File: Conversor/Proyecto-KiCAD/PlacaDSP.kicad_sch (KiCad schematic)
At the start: 0 parts

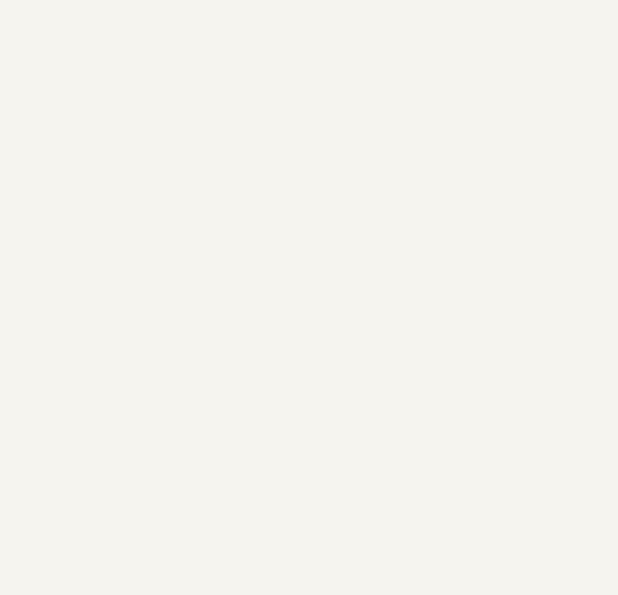
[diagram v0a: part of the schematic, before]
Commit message: Comenzar a pasar la placa adaptadora al proyecto
- Agregar a bibliografia info sobre la ControlCARD del TMS320F28335
(pinout del DIMM100 incluido)
- Agregar el proyecto importado a KiCad de la placa adaptadora
Por hacer:
  - Terminar de pasar la placa adaptadora, viendo que cosas no son
necesarias (como la entrada de 12V separada)
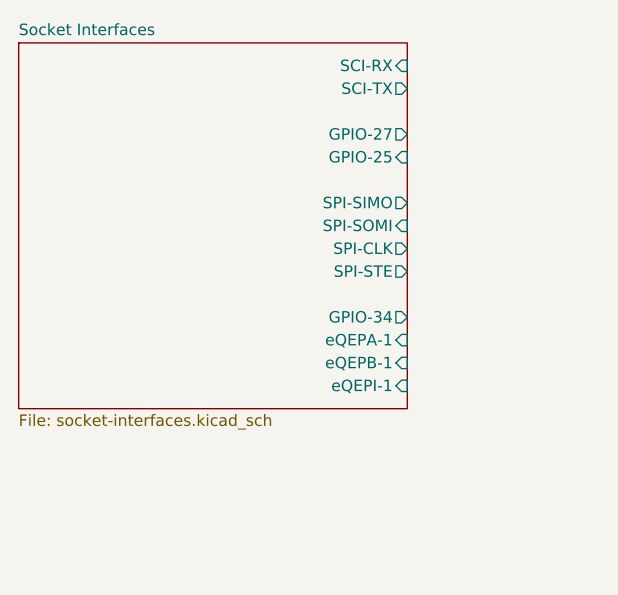
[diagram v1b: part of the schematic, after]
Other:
- added sheet Socket Interfaces (socket-interfaces.kicad_sch)
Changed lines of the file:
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@@
     (effects (font (size 2.54 2.54)) (justify right))
   )
+  (sheet (at 38.1 30.48) (size 43.18 40.64) (fields_autoplaced)
+    (stroke (width 0.1524) (type solid) (color 0 0 0 0))
+    (fill (color 0 0 0 0.0000))
+    (property "Sheet name" "Socket Interfaces" (id 0) (at 38.1 29.7684 0)
+      (effects (font (size 1.27 1.27)) (justify left bottom))
+    )
+    (property "Sheet file" "socket-interfaces.kicad_sch" (id 1) (at 38.1 71.7046 0)
+      (effects (font (size 1.27 1.27)) (justify left top))
+    )
+    (pin "SPI-CLK" output (at 81.28 53.34 0)
+      (effects (font (size 1.27 1.27)) (justify right))
+    )
+    (pin "SPI-STE" output (at 81.28 55.88 0)
+      (effects (font (size 1.27 1.27)) (justify right))
+    )
+    (pin "GPIO-27" output (at 81.28 40.64 0)
+      (effects (font (size 1.27 1.27)) (justify right))
+    )
+    (pin "SPI-SOMI" input (at 81.28 50.8 0)
+      (effects (font (size 1.27 1.27)) (justify right))
+    )
+    (pin "SPI-SIMO" output (at 81.28 48.26 0)
+      (effects (font (size 1.27 1.27)) (justify right))
+    )
+    (pin "eQEPI-1" input (at 81.28 68.58 0)
+      (effects (font (size 1.27 1.27)) (justify right))
+    )
+    (pin "eQEPA-1" input (at 81.28 63.5 0)
+      (effects (font (size 1.27 1.27)) (justify right))
+    )
+    (pin "eQEPB-1" input (at 81.28 66.04 0)
+      (effects (font (size 1.27 1.27)) (justify right))
+    )
+    (pin "SCI-TX" output (at 81.28 35.56 0)
+      (effects (font (size 1.27 1.27)) (justify right))
+    )
+    (pin "SCI-RX" input (at 81.28 33.02 0)
+      (effects (font (size 1.27 1.27)) (justify right))
+    )
+    (pin "GPIO-25" input (at 81.28 43.18 0)
+      (effects (font (size 1.27 1.27)) (justify right))
+    )
+    (pin "GPIO-34" output (at 81.28 60.96 0)
+      (effects (font (size 1.27 1.27)) (justify right))
+    )
+  )
 )

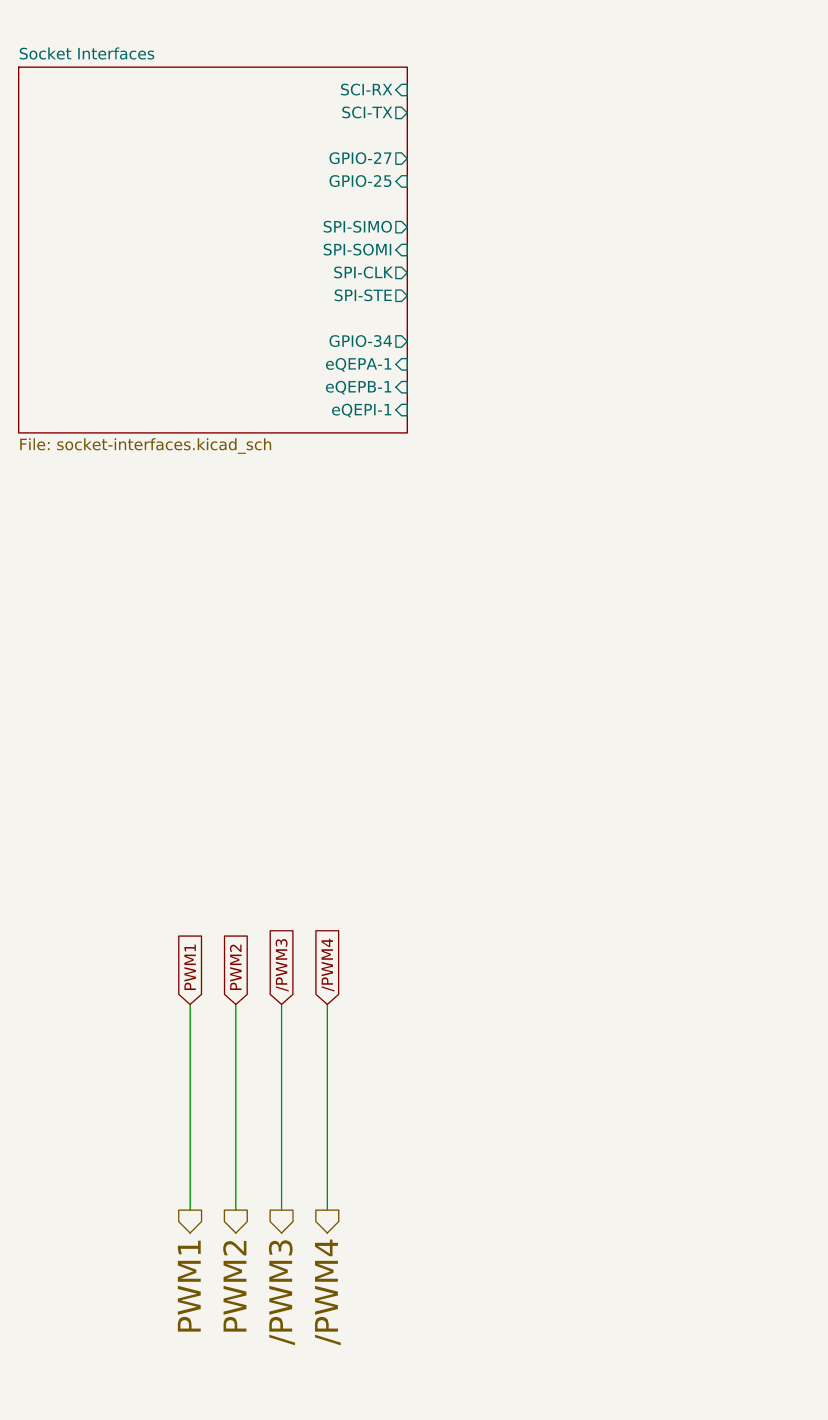
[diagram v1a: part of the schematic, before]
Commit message: Seleccionar componentes de los que me dieron y seguir con la placa adaptadora
- OpAmp OPA365AID para acondicionamiento de señales del sensor de efecto
hall
- Los optos que hay son ACPL-P343 en vez de P480, que necesitan 15-30V
de alimentación. Preguntar si no es mejor cambiarlos por 6N137, de 5V de
Vcc
- Regulador solo hay LM7805 de 5Vout pero también necesito 3.3Vout
- No hay ningún diodo en las cosas que me dieron

Por hacer:
  - Preguntar por los 6N137 y algun regulador de 3V3 out
  - Preguntar por los diodos del puente del conversor
  - Terminar de pasar la placa adaptadora del DSP
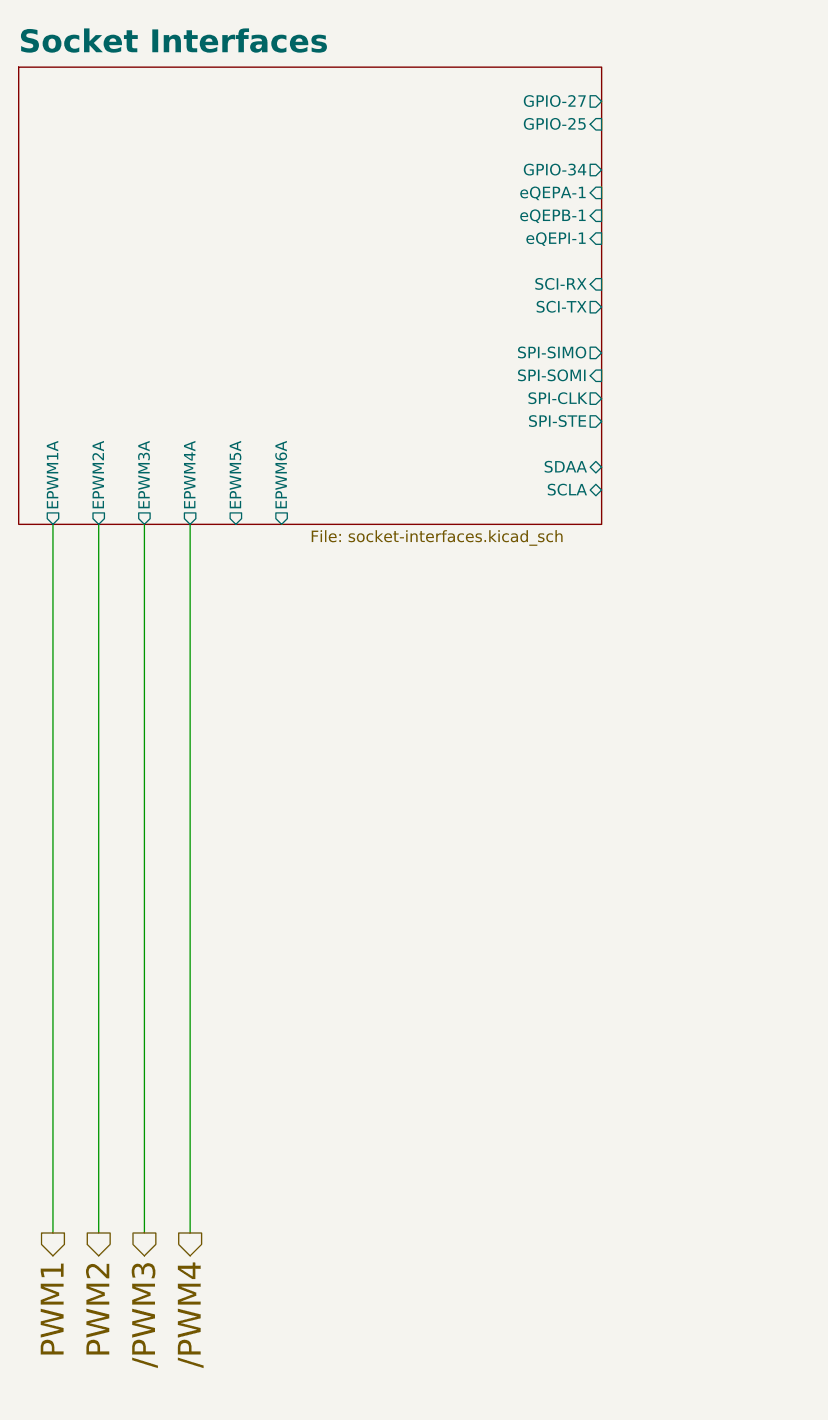
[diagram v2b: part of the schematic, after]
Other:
- sheet Socket Interfaces ports: added EPWM1A, EPWM2A, EPWM3A, EPWM4A, EPWM5A, EPWM6A, SCLA, SDAA; removed none
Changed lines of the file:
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@@
     (stroke (width 0) (type default) (color 0 0 0 0))
   )
-  (wire (pts (xy 57.15 134.62) (xy 57.15 157.48))
+  (wire (pts (xy 57.15 81.28) (xy 57.15 160.02))
     (stroke (width 0) (type default) (color 0 0 0 0))
   )
-  (wire (pts (xy 72.39 134.62) (xy 72.39 157.48))
+  (wire (pts (xy 52.07 81.28) (xy 52.07 160.02))
     (stroke (width 0) (type default) (color 0 0 0 0))
   )
-  (wire (pts (xy 62.23 134.62) (xy 62.23 157.48))
+  (wire (pts (xy 46.99 81.28) (xy 46.99 160.02))
+    (stroke (width 0) (type default) (color 0 0 0 0))
+  )
+  (wire (pts (xy 41.91 81.28) (xy 41.91 160.02))
     (stroke (width 0) (type default) (color 0 0 0 0))
   )
   (wire (pts (xy 219.71 63.5) (xy 238.76 63.5))
-    (stroke (width 0) (type default) (color 0 0 0 0))
-  )
-  (wire (pts (xy 67.31 134.62) (xy 67.31 157.48))
     (stroke (width 0) (type default) (color 0 0 0 0))
   )
@@
     (stroke (width 0) (type default) (color 0 0 0 0))
   )
-  (global_label "PWM2" (shape input) (at 62.23 134.62 90) (fields_autoplaced)
-    (effects (font (size 1.27 1.27)) (justify left))
-    (property "Intersheet References" "${INTERSHEET_REFS}" (id 0) (at 62.1506 126.8245 90)
-      (effects (font (size 1.27 1.27)) (justify left) hide)
-    )
-  )
-  (global_label "PWM1" (shape input) (at 57.15 134.62 90) (fields_autoplaced)
-    (effects (font (size 1.27 1.27)) (justify left))
-    (property "Intersheet References" "${INTERSHEET_REFS}" (id 0) (at 57.0706 126.8245 90)
-      (effects (font (size 1.27 1.27)) (justify left) hide)
-    )
-  )
   (global_label "ALARMIN" (shape output) (at 219.71 68.58 180) (fields_autoplaced)
     (effects (font (size 1.27 1.27)) (justify right))
@@
     (property "Intersheet References" "${INTERSHEET_REFS}" (id 0) (at 210.1002 78.6606 0)
       (effects (font (size 1.27 1.27)) (justify right) hide)
-    )
-  )
-  (global_label "{slash}PWM4" (shape input) (at 72.39 134.62 90) (fields_autoplaced)
-    (effects (font (size 1.27 1.27)) (justify left))
-    (property "Intersheet References" "${INTERSHEET_REFS}" (id 0) (at 72.3106 125.494 90)
-      (effects (font (size 1.27 1.27)) (justify left) hide)
     )
   )
@@
     )
   )
-  (global_label "{slash}PWM3" (shape input) (at 67.31 134.62 90) (fields_autoplaced)
-    (effects (font (size 1.27 1.27)) (justify left))
-    (property "Intersheet References" "${INTERSHEET_REFS}" (id 0) (at 67.2306 125.494 90)
-      (effects (font (size 1.27 1.27)) (justify left) hide)
-    )
-  )
   (hierarchical_label "DATAOUT" (shape output) (at 238.76 73.66 0)
     (effects (font (size 2.54 2.54)) (justify left))
@@
     (effects (font (size 2.54 2.54)) (justify left))
   )
-  (hierarchical_label "{slash}PWM4" (shape output) (at 72.39 157.48 270)
+  (hierarchical_label "{slash}PWM4" (shape output) (at 57.15 160.02 270)
     (effects (font (size 2.54 2.54)) (justify right))
   )
@@
     (effects (font (size 2.54 2.54)) (justify left))
   )
-  (hierarchical_label "{slash}PWM3" (shape output) (at 67.31 157.48 270)
+  (hierarchical_label "{slash}PWM3" (shape output) (at 52.07 160.02 270)
     (effects (font (size 2.54 2.54)) (justify right))
   )
-  (hierarchical_label "PWM2" (shape output) (at 62.23 157.48 270)
+  (hierarchical_label "PWM2" (shape output) (at 46.99 160.02 270)
     (effects (font (size 2.54 2.54)) (justify right))
   )
@@
     (effects (font (size 2.54 2.54)) (justify left))
   )
-  (hierarchical_label "PWM1" (shape output) (at 57.15 157.48 270)
+  (hierarchical_label "PWM1" (shape output) (at 41.91 160.02 270)
     (effects (font (size 2.54 2.54)) (justify right))
   )
-  (sheet (at 38.1 30.48) (size 43.18 40.64) (fields_autoplaced)
+  (sheet (at 38.1 30.48) (size 64.77 50.8)
     (stroke (width 0.1524) (type solid) (color 0 0 0 0))
     (fill (color 0 0 0 0.0000))
-    (property "Sheet name" "Socket Interfaces" (id 0) (at 38.1 29.7684 0)
-      (effects (font (size 1.27 1.27)) (justify left bottom))
+    (property "Sheet name" "Socket Interfaces" (id 0) (at 38.1 29.1334 0)
+      (effects (font (size 2.54 2.54) bold) (justify left bottom))
     )
-    (property "Sheet file" "socket-interfaces.kicad_sch" (id 1) (at 38.1 71.7046 0)
+    (property "Sheet file" "socket-interfaces.kicad_sch" (id 1) (at 70.485 81.915 0)
       (effects (font (size 1.27 1.27)) (justify left top))
     )
-    (pin "SPI-CLK" output (at 81.28 53.34 0)
+    (pin "SPI-CLK" output (at 102.87 67.31 0)
       (effects (font (size 1.27 1.27)) (justify right))
     )
-    (pin "SPI-STE" output (at 81.28 55.88 0)
+    (pin "SPI-STE" output (at 102.87 69.85 0)
       (effects (font (size 1.27 1.27)) (justify right))
     )
-    (pin "GPIO-27" output (at 81.28 40.64 0)
+    (pin "GPIO-27" output (at 102.87 34.29 0)
       (effects (font (size 1.27 1.27)) (justify right))
     )
-    (pin "SPI-SOMI" input (at 81.28 50.8 0)
+    (pin "SPI-SOMI" input (at 102.87 64.77 0)
       (effects (font (size 1.27 1.27)) (justify right))
     )
-    (pin "SPI-SIMO" output (at 81.28 48.26 0)
+    (pin "SPI-SIMO" output (at 102.87 62.23 0)
       (effects (font (size 1.27 1.27)) (justify right))
     )
-    (pin "eQEPI-1" input (at 81.28 68.58 0)
+    (pin "eQEPI-1" input (at 102.87 49.53 0)
       (effects (font (size 1.27 1.27)) (justify right))
     )
-    (pin "eQEPA-1" input (at 81.28 63.5 0)
+    (pin "eQEPA-1" input (at 102.87 44.45 0)
       (effects (font (size 1.27 1.27)) (justify right))
     )
-    (pin "eQEPB-1" input (at 81.28 66.04 0)
+    (pin "eQEPB-1" input (at 102.87 46.99 0)
       (effects (font (size 1.27 1.27)) (justify right))
     )
-    (pin "SCI-TX" output (at 81.28 35.56 0)
+    (pin "SCI-TX" output (at 102.87 57.15 0)
       (effects (font (size 1.27 1.27)) (justify right))
     )
-    (pin "SCI-RX" input (at 81.28 33.02 0)
+    (pin "SCI-RX" input (at 102.87 54.61 0)
       (effects (font (size 1.27 1.27)) (justify right))
     )
-    (pin "GPIO-25" input (at 81.28 43.18 0)
+    (pin "GPIO-25" input (at 102.87 36.83 0)
       (effects (font (size 1.27 1.27)) (justify right))
     )
-    (pin "GPIO-34" output (at 81.28 60.96 0)
+    (pin "GPIO-34" output (at 102.87 41.91 0)
       (effects (font (size 1.27 1.27)) (justify right))
     )
+    (pin "EPWM5A" output (at 62.23 81.28 270)
+      (effects (font (size 1.27 1.27)) (justify left))
+    )
+    (pin "EPWM4A" output (at 57.15 81.28 270)
+      (effects (font (size 1.27 1.27)) (justify left))
+    )
+    (pin "EPWM3A" output (at 52.07 81.28 270)
+      (effects (font (size 1.27 1.27)) (justify left))
+    )
+    (pin "EPWM1A" output (at 41.91 81.28 270)
+      (effects (font (size 1.27 1.27)) (justify left))
+    )
+    (pin "EPWM2A" output (at 46.99 81.28 270)
+      (effects (font (size 1.27 1.27)) (justify left))
+    )
+    (pin "EPWM6A" output (at 67.31 81.28 270)
+      (effects (font (size 1.27 1.27)) (justify left))
+    )
+    (pin "SDAA" bidirectional (at 102.87 74.93 0)
+      (effects (font (size 1.27 1.27)) (justify right))
+    )
+    (pin "SCLA" bidirectional (at 102.87 77.47 0)
+      (effects (font (size 1.27 1.27)) (justify right))
+    )
